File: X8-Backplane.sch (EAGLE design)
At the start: 32 parts, among them U1 BD6221FSOP, U4 FQB27P06, U5 FQB27P06, U6 FQB27P06, U7 LM2678

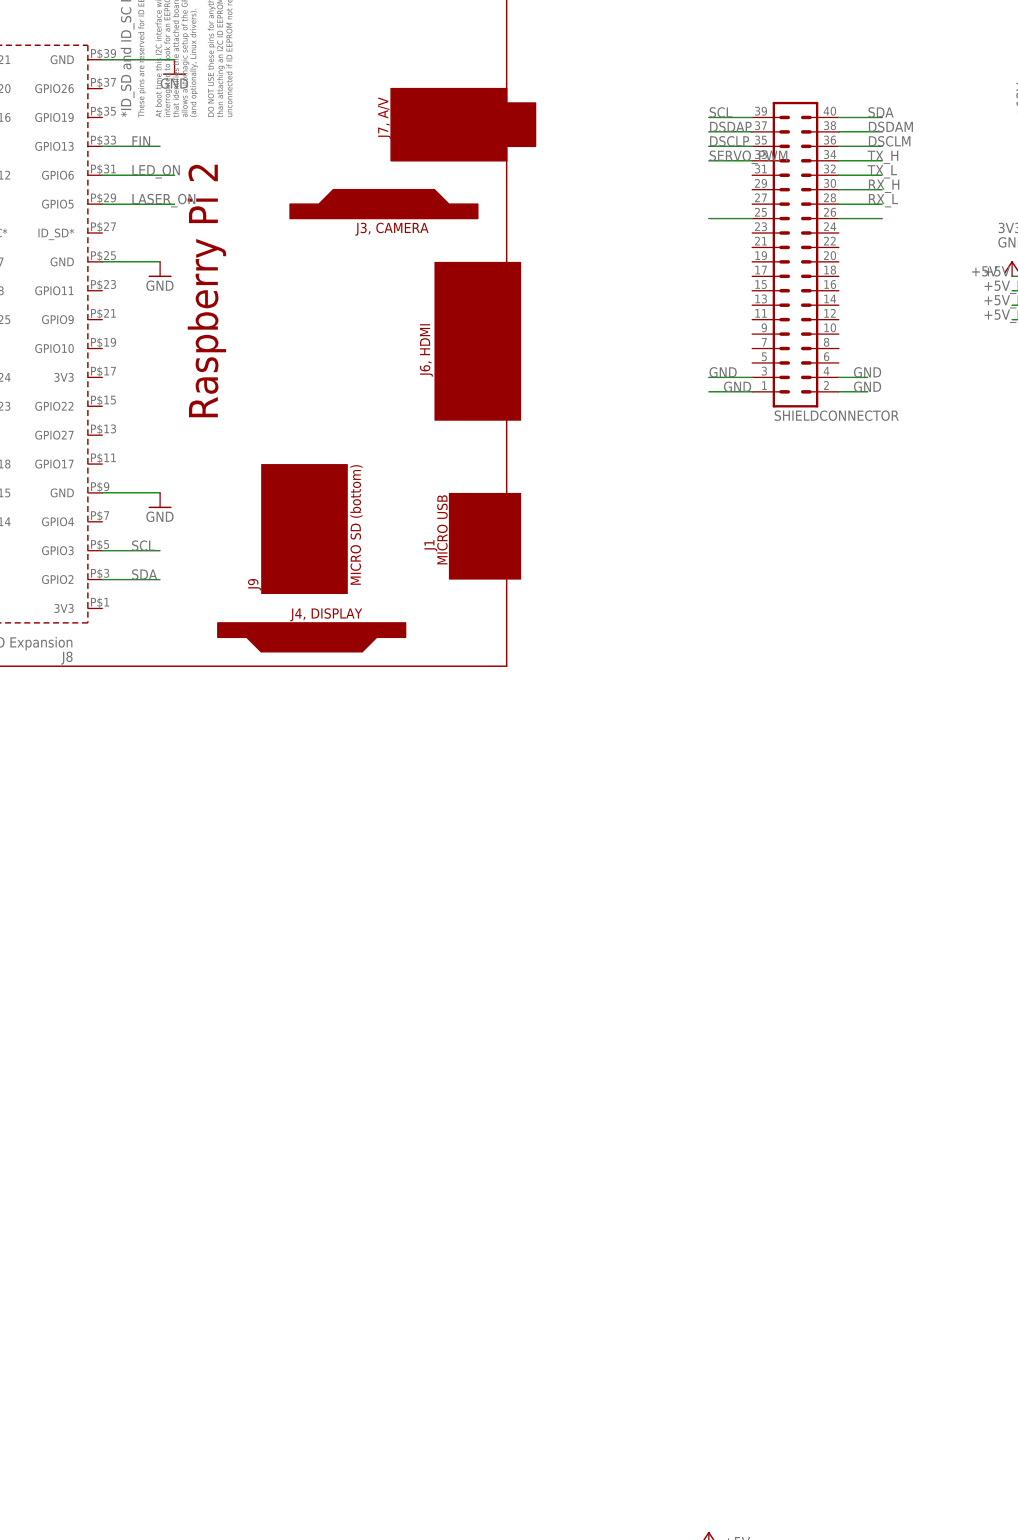
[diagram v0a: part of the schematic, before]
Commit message: added SPI to UART ship
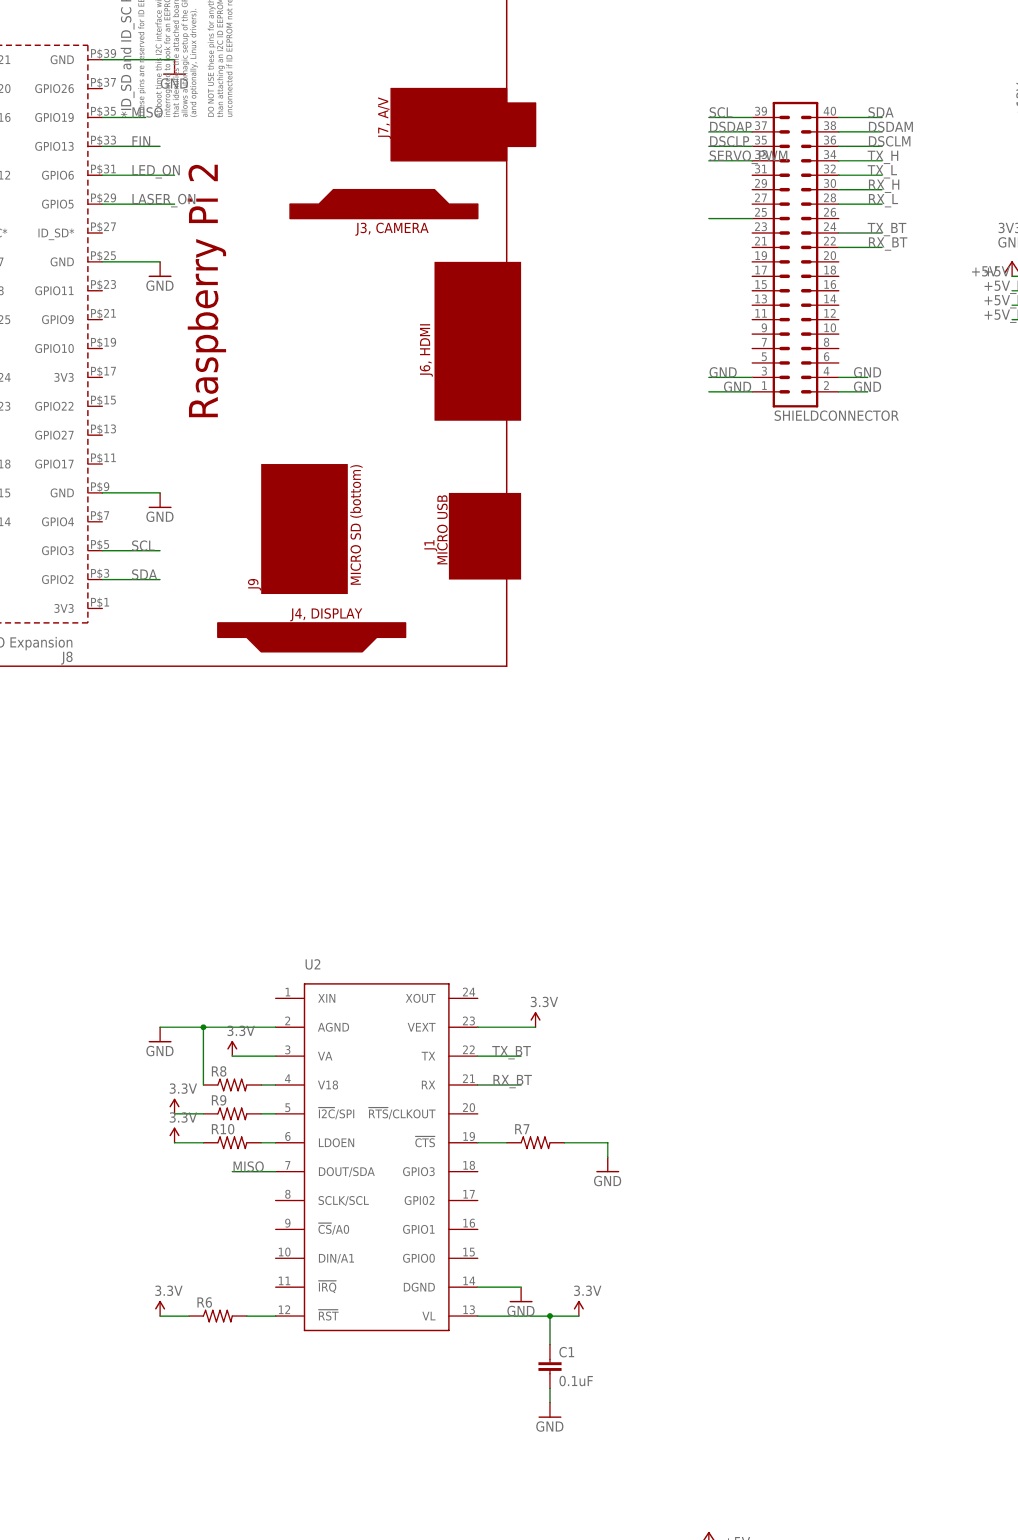
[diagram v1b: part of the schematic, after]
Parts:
- added C1: 0.1uF, SparkFun-Capacitors:0.1UF-25V(+80/-20%)(0603)
- added R10, R6, R7, R8, R9: (no value), SparkFun-Passives:RESISTOR0603-RES
- added U2: (no value), BackplaneParts:MAX3107SSOP
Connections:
- new net MISO: PCB1.GPIO19, U2.DOUT/SDA
- new net N$10: R9.2, U2.!I2C!/SPI
- new net N$12: R10.2, U2.LDOEN
- new net N$7: R6.2, U2.!RST!
- new net N$8: R7.1, U2.!CTS!
- new net N$9: R8.2, U2.V18
- new net RX_BT: U$4G$1.21, U2.RX
- new net TX_BT: U$4G$1.23, U2.TX
- net 3.3V: now also C1.1, R10.1, R6.1, R9.1, U2.VA, U2.VEXT, U2.VL; no longer U$4G$1.25
- net GND: now also C1.2, R7.2, R8.1, U2.AGND, U2.DGND
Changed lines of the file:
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@@
 <part name="GND19" library="SparkFun-Aesthetics" deviceset="GND" device=""/>
 <part name="P+3" library="supply1" deviceset="+12V" device=""/>
+<part name="U2" library="BackplaneParts" deviceset="MAX3107" device="SSOP"/>
+<part name="GND20" library="supply1" deviceset="GND" device=""/>
+<part name="GND21" library="supply1" deviceset="GND" device=""/>
+<part name="R6" library="SparkFun-Passives" deviceset="RESISTOR" device="0603-RES"/>
+<part name="SUPPLY5" library="SparkFun-Aesthetics" deviceset="3.3V" device=""/>
+<part name="SUPPLY6" library="SparkFun-Aesthetics" deviceset="3.3V" device=""/>
+<part name="C1" library="SparkFun-Capacitors" deviceset="0.1UF-25V(+80/-20%)(0603)" device="" value="0.1uF"/>
+<part name="GND22" library="supply1" deviceset="GND" device=""/>
+<part name="R7" library="SparkFun-Passives" deviceset="RESISTOR" device="0603-RES"/>
+<part name="GND23" library="supply1" deviceset="GND" device=""/>
+<part name="SUPPLY7" library="SparkFun-Aesthetics" deviceset="3.3V" device=""/>
+<part name="R8" library="SparkFun-Passives" deviceset="RESISTOR" device="0603-RES"/>
+<part name="SUPPLY8" library="SparkFun-Aesthetics" deviceset="3.3V" device=""/>
+<part name="R9" library="SparkFun-Passives" deviceset="RESISTOR" device="0603-RES"/>
+<part name="SUPPLY9" library="SparkFun-Aesthetics" deviceset="3.3V" device=""/>
+<part name="SUPPLY10" library="SparkFun-Aesthetics" deviceset="3.3V" device=""/>
+<part name="R10" library="SparkFun-Passives" deviceset="RESISTOR" device="0603-RES"/>
 </parts>
 <sheets>
@@
 <instance part="GND19" gate="1" x="17.78" y="-152.4"/>
 <instance part="P+3" gate="1" x="17.78" y="-111.76"/>
+<instance part="U2" gate="G$1" x="116.84" y="-53.34"/>
+<instance part="GND20" gate="1" x="78.74" y="-33.02"/>
+<instance part="GND21" gate="1" x="142.24" y="-78.74"/>
+<instance part="R6" gate="G$1" x="88.9" y="-81.28"/>
+<instance part="SUPPLY5" gate="G$1" x="78.74" y="-81.28"/>
+<instance part="SUPPLY6" gate="G$1" x="152.4" y="-81.28"/>
+<instance part="C1" gate="G$1" x="147.32" y="-91.44"/>
+<instance part="GND22" gate="1" x="147.32" y="-99.06"/>
+<instance part="R7" gate="G$1" x="144.78" y="-50.8"/>
+<instance part="GND23" gate="1" x="157.48" y="-55.88"/>
+<instance part="SUPPLY7" gate="G$1" x="144.78" y="-30.48"/>
+<instance part="R8" gate="G$1" x="91.44" y="-40.64"/>
+<instance part="SUPPLY8" gate="G$1" x="91.44" y="-35.56"/>
+<instance part="R9" gate="G$1" x="91.44" y="-45.72"/>
+<instance part="SUPPLY9" gate="G$1" x="81.28" y="-45.72"/>
+<instance part="SUPPLY10" gate="G$1" x="81.28" y="-50.8"/>
+<instance part="R10" gate="G$1" x="91.44" y="-50.8"/>
 </instances>
 <busses>
@@
 <wire x1="17.78" y1="-144.78" x2="17.78" y2="-149.86" width="0.1524" layer="91"/>
 </segment>
+<segment>
+<pinref part="U2" gate="G$1" pin="DGND"/>
+<pinref part="GND21" gate="1" pin="GND"/>
+<wire x1="134.62" y1="-76.2" x2="142.24" y2="-76.2" width="0.1524" layer="91"/>
+</segment>
+<segment>
+<pinref part="U2" gate="G$1" pin="AGND"/>
+<pinref part="GND20" gate="1" pin="GND"/>
+<wire x1="99.06" y1="-30.48" x2="86.36" y2="-30.48" width="0.1524" layer="91"/>
+<pinref part="R8" gate="G$1" pin="1"/>
+<wire x1="86.36" y1="-30.48" x2="78.74" y2="-30.48" width="0.1524" layer="91"/>
+<wire x1="86.36" y1="-40.64" x2="86.36" y2="-30.48" width="0.1524" layer="91"/>
+<junction x="86.36" y="-30.48"/>
+</segment>
+<segment>
+<pinref part="C1" gate="G$1" pin="2"/>
+<pinref part="GND22" gate="1" pin="GND"/>
+<wire x1="147.32" y1="-93.98" x2="147.32" y2="-96.52" width="0.1524" layer="91"/>
+</segment>
+<segment>
+<pinref part="R7" gate="G$1" pin="2"/>
+<pinref part="GND23" gate="1" pin="GND"/>
+<wire x1="149.86" y1="-50.8" x2="157.48" y2="-50.8" width="0.1524" layer="91"/>
+<wire x1="157.48" y1="-50.8" x2="157.48" y2="-53.34" width="0.1524" layer="91"/>
+</segment>
 </net>
 <net name="+12V" class="0">
@@
 </segment>
 <segment>
-<pinref part="U$4" gate="G$1" pin="25"/>
-<wire x1="198.12" y1="111.76" x2="205.74" y2="111.76" width="0.1524" layer="91"/>
+<pinref part="R6" gate="G$1" pin="1"/>
+<pinref part="SUPPLY5" gate="G$1" pin="3.3V"/>
+<wire x1="83.82" y1="-81.28" x2="78.74" y2="-81.28" width="0.1524" layer="91"/>
+</segment>
+<segment>
+<pinref part="U2" gate="G$1" pin="VL"/>
+<pinref part="SUPPLY6" gate="G$1" pin="3.3V"/>
+<wire x1="134.62" y1="-81.28" x2="147.32" y2="-81.28" width="0.1524" layer="91"/>
+<pinref part="C1" gate="G$1" pin="1"/>
+<wire x1="147.32" y1="-81.28" x2="152.4" y2="-81.28" width="0.1524" layer="91"/>
+<wire x1="147.32" y1="-81.28" x2="147.32" y2="-86.36" width="0.1524" layer="91"/>
+<junction x="147.32" y="-81.28"/>
+</segment>
+<segment>
+<pinref part="U2" gate="G$1" pin="VEXT"/>
+<pinref part="SUPPLY7" gate="G$1" pin="3.3V"/>
+<wire x1="134.62" y1="-30.48" x2="144.78" y2="-30.48" width="0.1524" layer="91"/>
+</segment>
+<segment>
+<pinref part="SUPPLY8" gate="G$1" pin="3.3V"/>
+<pinref part="U2" gate="G$1" pin="VA"/>
+<wire x1="91.44" y1="-35.56" x2="99.06" y2="-35.56" width="0.1524" layer="91"/>
+</segment>
+<segment>
+<pinref part="R9" gate="G$1" pin="1"/>
+<pinref part="SUPPLY9" gate="G$1" pin="3.3V"/>
+<wire x1="86.36" y1="-45.72" x2="81.28" y2="-45.72" width="0.1524" layer="91"/>
+</segment>
+<segment>
+<wire x1="86.36" y1="-50.8" x2="81.28" y2="-50.8" width="0.1524" layer="91"/>
+<pinref part="SUPPLY10" gate="G$1" pin="3.3V"/>
+<pinref part="R10" gate="G$1" pin="1"/>
 </segment>
 </net>
@@
 </segment>
 </net>
+<net name="N$7" class="0">
+<segment>
+<pinref part="R6" gate="G$1" pin="2"/>
+<pinref part="U2" gate="G$1" pin="!RST!"/>
+<wire x1="93.98" y1="-81.28" x2="99.06" y2="-81.28" width="0.1524" layer="91"/>
+</segment>
+</net>
+<net name="N$8" class="0">
+<segment>
+<pinref part="U2" gate="G$1" pin="!CTS!"/>
+<pinref part="R7" gate="G$1" pin="1"/>
+<wire x1="134.62" y1="-50.8" x2="139.7" y2="-50.8" width="0.1524" layer="91"/>
+</segment>
+</net>
+<net name="TX_BT" class="0">
+<segment>
+<pinref part="U$4" gate="G$1" pin="23"/>
+<wire x1="198.12" y1="109.22" x2="205.74" y2="109.22" width="0.1524" layer="91"/>
+<label x="203.2" y="109.22" size="1.778" layer="95"/>
+</segment>
+<segment>
+<pinref part="U2" gate="G$1" pin="TX"/>
+<wire x1="134.62" y1="-35.56" x2="142.24" y2="-35.56" width="0.1524" layer="91"/>
+<label x="137.16" y="-35.56" size="1.778" layer="95"/>
+</segment>
+</net>
+<net name="RX_BT" class="0">
+<segment>
+<pinref part="U$4" gate="G$1" pin="21"/>
+<wire x1="198.12" y1="106.68" x2="205.74" y2="106.68" width="0.1524" layer="91"/>
+<label x="203.2" y="106.68" size="1.778" layer="95"/>
+</segment>
+<segment>
+<pinref part="U2" gate="G$1" pin="RX"/>
+<wire x1="134.62" y1="-40.64" x2="142.24" y2="-40.64" width="0.1524" layer="91"/>
+<label x="137.16" y="-40.64" size="1.778" layer="95"/>
+</segment>
+</net>
+<net name="N$9" class="0">
+<segment>
+<pinref part="U2" gate="G$1" pin="V18"/>
+<pinref part="R8" gate="G$1" pin="2"/>
+<wire x1="99.06" y1="-40.64" x2="96.52" y2="-40.64" width="0.1524" layer="91"/>
+</segment>
+</net>
+<net name="N$10" class="0">
+<segment>
+<pinref part="U2" gate="G$1" pin="!I2C!/SPI"/>
+<pinref part="R9" gate="G$1" pin="2"/>
+<wire x1="99.06" y1="-45.72" x2="96.52" y2="-45.72" width="0.1524" layer="91"/>
+</segment>
+</net>
+<net name="N$12" class="0">
+<segment>
+<pinref part="U2" gate="G$1" pin="LDOEN"/>
+<pinref part="R10" gate="G$1" pin="2"/>
+<wire x1="96.52" y1="-50.8" x2="99.06" y2="-50.8" width="0.1524" layer="91"/>
+</segment>
+</net>
+<net name="MISO" class="0">
+<segment>
+<pinref part="PCB1" gate="G$1" pin="GPIO19"/>
+<wire x1="68.58" y1="129.54" x2="76.2" y2="129.54" width="0.1524" layer="91"/>
+<label x="73.66" y="129.54" size="1.778" layer="95"/>
+</segment>
+<segment>
+<pinref part="U2" gate="G$1" pin="DOUT/SDA"/>
+<wire x1="99.06" y1="-55.88" x2="91.44" y2="-55.88" width="0.1524" layer="91"/>
+<label x="91.44" y="-55.88" size="1.778" layer="95"/>
+</segment>
+</net>
